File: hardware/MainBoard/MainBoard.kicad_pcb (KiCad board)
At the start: 4 copper layers, 28 x 58.4 mm, 53 parts, among them J1 Conn_02x16_Top_Bottom, J2 Conn_02x16_Top_Bottom, J3 USB_C_Receptacle_USB2.0_16P, J4 En_A, J5 En_B, J6 Micro_SD_Card_Det2, J7 Conn_02x16_Top_Bottom, Q1 MMBT2222A, U2 AMS1117-3.3, U3 AMS1117-5.0

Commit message: made boards actually square lmao
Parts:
- renumbered ESP32-S3-WROOM-1 to U1
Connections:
- C10 pad 1: CONN_VCC -> VCC_5V
- C11 pad 1: CONN_VCC -> VCC_5V
- C12 pad 1: CONN_VCC -> VCC_5V
- D4 pad 1: CONN_VCC -> VCC_5V
- Q1 pad 3: CONN_VCC -> VCC_5V
- R3 pad 1: CONN_VCC -> VCC_5V
- U3 pad 2: CONN_VCC -> VCC_5V
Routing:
- net CONN_VCC: track 103.0 -> 67.3 mm, vias 15 -> 14
- net VCC_5V: track 0.00 -> 7.69 mm, vias 0 -> 1
- added copper zone on In1.Cu, net CONN_GND
- added copper zone on In2.Cu, net CONN_VCC
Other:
- outline, holes or cut-outs redrawn

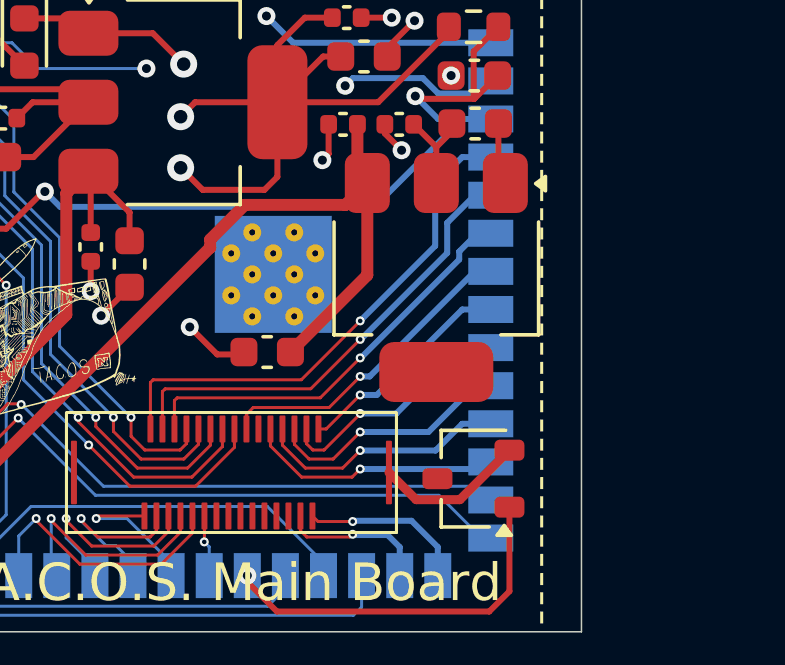
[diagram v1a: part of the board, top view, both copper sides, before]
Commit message: finished main board w/ ground and power planes
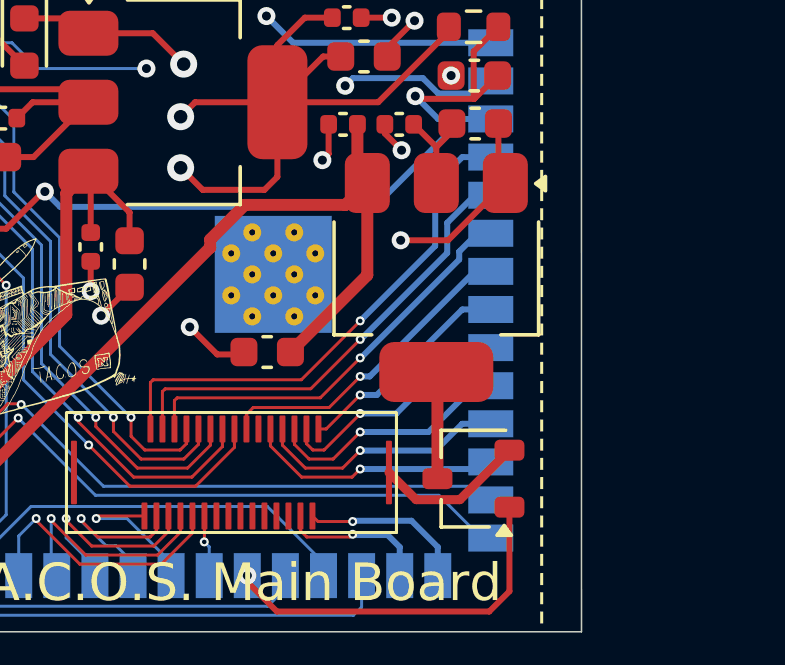
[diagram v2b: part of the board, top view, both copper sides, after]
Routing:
- net CONN_GND: track 88.8 -> 93.0 mm, vias 30 -> 31
- net VCC_5V: track 7.69 -> 11.2 mm
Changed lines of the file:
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@@
+	)
+	(segment
+		(start 87.9628 61.3156)
+		(end 86.0534 63.225)
+		(width 0.2)
+		(layer "F.Cu")
+		(net 70)
 	)
 	(segment
@@
 		(start 67.7416 90.0616)
 		(end 67.36 89.68)
+		(width 0.2)
+		(layer "F.Cu")
+		(net 70)
+	)
+	(segment
+		(start 86.0534 63.225)
+		(end 84.475 63.225)
 		(width 0.2)
 		(layer "F.Cu")
@@
 	)
 	(via
+		(at 84.475 63.225)
+		(size 0.6)
+		(drill 0.3)
+		(layers "F.Cu" "B.Cu")
+		(net 70)
+	)
+	(via
 		(at 67.29 97.55)
 		(size 0.3)
@@
 	)
 	(segment
+		(start 85.6628 60.1156)
+		(end 84.907 59.3598)
+		(width 0.2)
+		(layer "F.Cu")
+		(net 76)
+	)
+	(segment
+		(start 65.3542 91.4654)
+		(end 64.6938 90.805)
+		(width 0.2)
+		(layer "F.Cu")
+		(net 76)
+	)
+	(segment
+		(start 66.294 88.519)
+		(end 66.294 87.336)
+		(width 0.2)
+		(layer "F.Cu")
+		(net 76)
+	)
+	(segment
+		(start 86.1822 59.3344)
+		(end 86.1822 59.5962)
+		(width 0.2)
+		(layer "F.Cu")
+		(net 76)
+	)
+	(segment
+		(start 65.3542 92.329)
+		(end 65.3542 91.4654)
+		(width 0.2)
+		(layer "F.Cu")
+		(net 76)
+	)
+	(segment
+		(start 85.6628 61.3156)
+		(end 85.6628 60.1156)
+		(width 0.2)
+		(layer "F.Cu")
+		(net 76)
+	)
+	(segment
+		(start 66.294 87.336)
+		(end 67.28 86.35)
+		(width 0.2)
+		(layer "F.Cu")
+		(net 76)
+	)
+	(segment
+		(start 85.7003 71.1708)
+		(end 85.7003 67.6531)
+		(width 0.4)
+		(layer "F.Cu")
+		(net 76)
+	)
+	(segment
 		(start 85.7003 67.6531)
 		(end 85.6628 67.6156)
-		(width 0.2)
+		(width 0.4)
 		(layer "F.Cu")
 		(net 76)
-	)
-	(segment
-		(start 85.6628 60.1156)
-		(end 84.907 59.3598)
-		(width 0.2)
-		(layer "F.Cu")
-		(net 76)
-	)
-	(segment
-		(start 65.3542 91.4654)
-		(end 64.6938 90.805)
-		(width 0.2)
-		(layer "F.Cu")
-		(net 76)
-	)
-	(segment
-		(start 66.294 88.519)
-		(end 66.294 87.336)
-		(width 0.2)
-		(layer "F.Cu")
-		(net 76)
-	)
-	(segment
-		(start 86.1822 59.3344)
-		(end 86.1822 59.5962)
-		(width 0.2)
-		(layer "F.Cu")
-		(net 76)
-	)
-	(segment
-		(start 65.3542 92.329)
-		(end 65.3542 91.4654)
-		(width 0.2)
-		(layer "F.Cu")
-		(net 76)
-	)
-	(segment
-		(start 85.6628 61.3156)
-		(end 85.6628 60.1156)
-		(width 0.2)
-		(layer "F.Cu")
-		(net 76)
-	)
-	(segment
-		(start 66.294 87.336)
-		(end 67.28 86.35)
-		(width 0.2)
-		(layer "F.Cu")
-		(net 76)

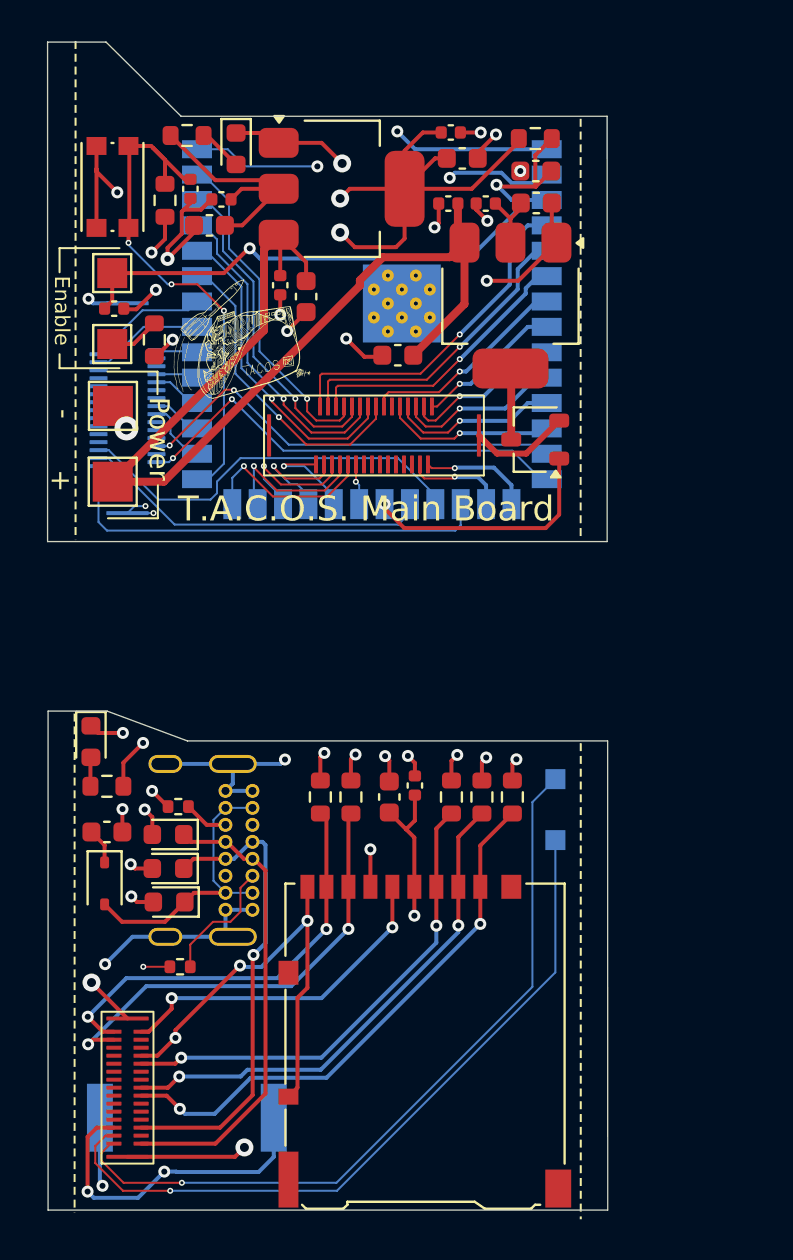
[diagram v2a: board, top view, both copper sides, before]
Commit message: added USB power switching
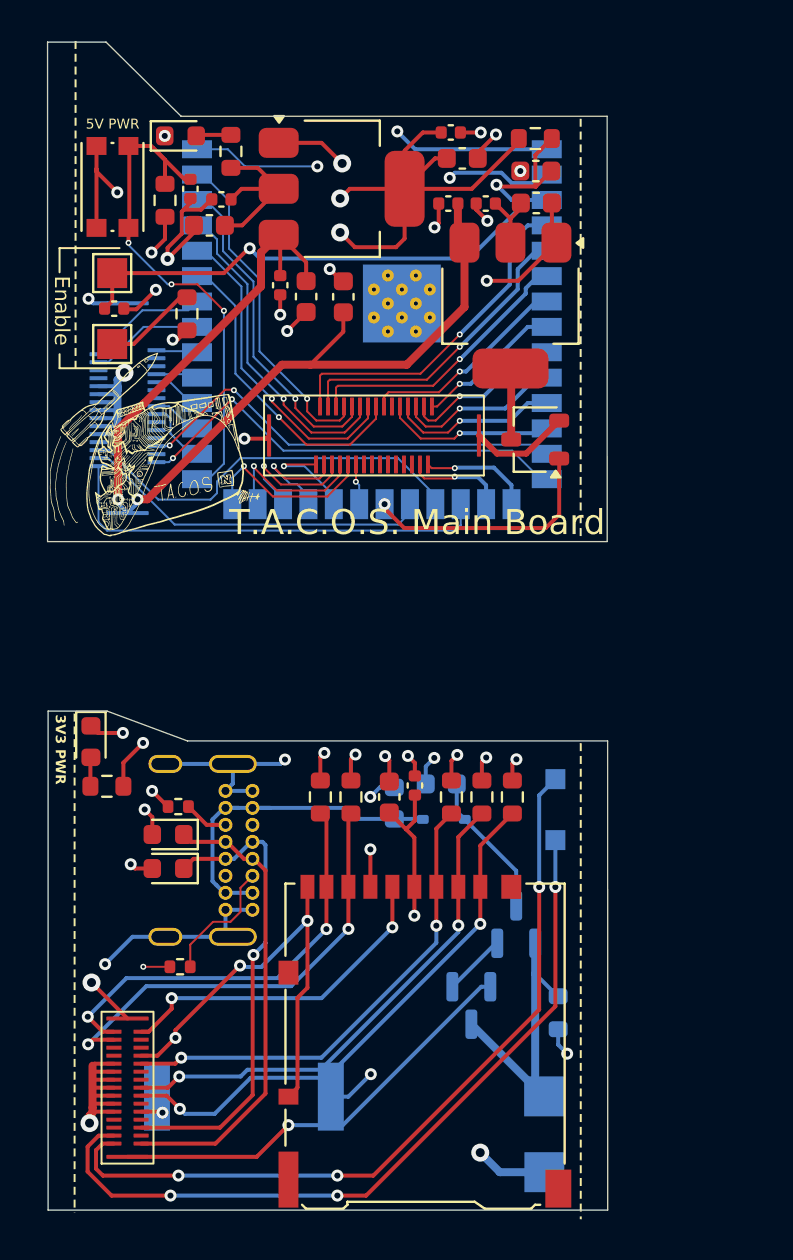
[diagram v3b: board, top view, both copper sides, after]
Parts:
- added Q2: FDN340P, Package_TO_SOT_SMD:SOT-23, B.Cu at (86.0, 95.4)
- added Q3: FDN340P, Package_TO_SOT_SMD:SOT-23, B.Cu at (83.7, 99.5)
- added R13: 10K, Resistor_SMD:R_0603_1608Metric, B.Cu at (88.0, 99.8)
- +1, -1, C12, D3, D4: moved to B.Cu
- moved -1 44.0 mm to (87.4, 107.8)
- moved +1 37.6 mm to (87.3, 104.0)
- moved D4 17.3 mm to (82.3, 90.2), turned to 180 degrees
- moved C12 16.9 mm to (82.2, 88.4), turned to 180 degrees
- moved D3 12.3 mm to (79.8, 89.4), turned to 90 degrees
- moved G*** 6.85 mm to (70.8, 61.8)
- moved C8 4.00 mm to (77.3, 64.0), turned to 90 degrees
- moved BZ1 3.04 mm to (72.3, 104.0), turned to 0 degrees
- moved D1 2.86 mm to (69.2, 56.0), turned to 0 degrees
- moved G*** 2.80 mm to (75.3, 85.0)
- moved R2 2.33 mm to (71.7, 56.8), turned to 90 degrees
- moved R12 2.09 mm to (69.5, 64.9)
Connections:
- net CONN_GND renamed LIPO GND
- C12 pad 1: VCC_5V -> VBUS
- C13 pad 1: CONN_VCC -> CONN_19
- C15 pad 1: CONN_VCC -> CONN_19
- C2 pad 1: CONN_VCC -> CONN_19
- C3 pad 1: CONN_VCC -> CONN_19
- C4 pad 1: LIPO PWR -> VIN
- C5 pad 1: LIPO PWR -> VIN
- C6 pad 1: CONN_VCC -> CONN_19
- C7 pad 1: CONN_VCC -> CONN_19
- C8 pad 1: LIPO PWR -> VIN
- C9 pad 1: LIPO PWR -> VIN
- D4 pad 1: VCC_5V -> VBUS
- J1 pad 18: BZR -> CONN_17
- J1 pad 21: CONN_20 -> CONN_19
- J1 pad 22: CONN_21 -> CONN_19
- J1 pad 23: CONN_22 -> CONN_19
- J1 pad 24: CONN_23 -> CONN_19
- J1 pad 25: CONN_24 -> CONN_19
- J1 pad 26: CONN_25 -> CONN_19
- J1 pad 31: CONN_VCC -> VIN
- J1 pad 5: CONN_4 -> BZR
- J2 pad 10: CONN_24 -> CONN_19
- J2 pad 11: CONN_25 -> CONN_19
- J2 pad 20: CONN_4 -> BZR
- J2 pad 3: BZR -> CONN_17
- J2 pad 31: CONN_VCC -> VIN
- J2 pad 6: CONN_20 -> CONN_19
- J2 pad 7: CONN_21 -> CONN_19
- J2 pad 8: CONN_22 -> CONN_19
- J2 pad 9: CONN_23 -> CONN_19
- J6 pad 4: CONN_VCC -> CONN_19
- J7 pad 31: CONN_5V -> VCC_5V
- R1 pad 1: CONN_VCC -> CONN_19
- R10 pad 1: CONN_VCC -> CONN_19
- R11 pad 1: CONN_VCC -> CONN_19
- R12 pad 1: CONN_VCC -> CONN_19
- R2 pad 1: CONN_VCC -> CONN_19
- R6 pad 1: CONN_VCC -> CONN_19
- R7 pad 1: CONN_VCC -> CONN_19
- R8 pad 1: CONN_VCC -> CONN_19
- R9 pad 1: CONN_VCC -> CONN_19
- U1 pad 2: CONN_VCC -> CONN_19
- U2 pad 2: CONN_VCC -> CONN_19
- U2 pad 3: LIPO PWR -> VIN
- U3 pad 3: LIPO PWR -> VIN
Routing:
- net CONN_19: track 0.00 -> 76.0 mm, vias 0 -> 13
- net VIN: track 0.00 -> 74.6 mm, vias 0 -> 3
- net CONN_VCC: track 67.3 -> 0.00 mm, vias 14 -> 0
- net LIPO PWR: track 52.5 -> 14.6 mm
- net BZR: track 36.8 -> 21.4 mm, vias 2 -> 1
- net VBUS: track 0.00 -> 7.33 mm
- net Net-(D3-A1): track 14.5 -> 17.9 mm
- net +5V: track 0.00 -> 3.15 mm
- net CONN_16: track 54.4 -> 56.6 mm, vias 1 -> 3
- net Net-(J4-Pin_1): track 2.54 -> 4.71 mm
- net VCC_5V: track 11.2 -> 9.41 mm
- net CONN_15: track 60.4 -> 61.9 mm, vias 1 -> 3
- net LIPO GND: track 93.0 -> 93.7 mm, vias 31 -> 34
- added copper zone on In2.Cu, net CONN_19
- removed copper zone on In2.Cu, net CONN_VCC
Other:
- board text added: "3V3 PWR"
- board text added: "5V PWR"
- board text added: "CLK"
- board text added: "DAT"
- board text added: "ESP32-S3-WROOM-1"
- board text added: "I2C"

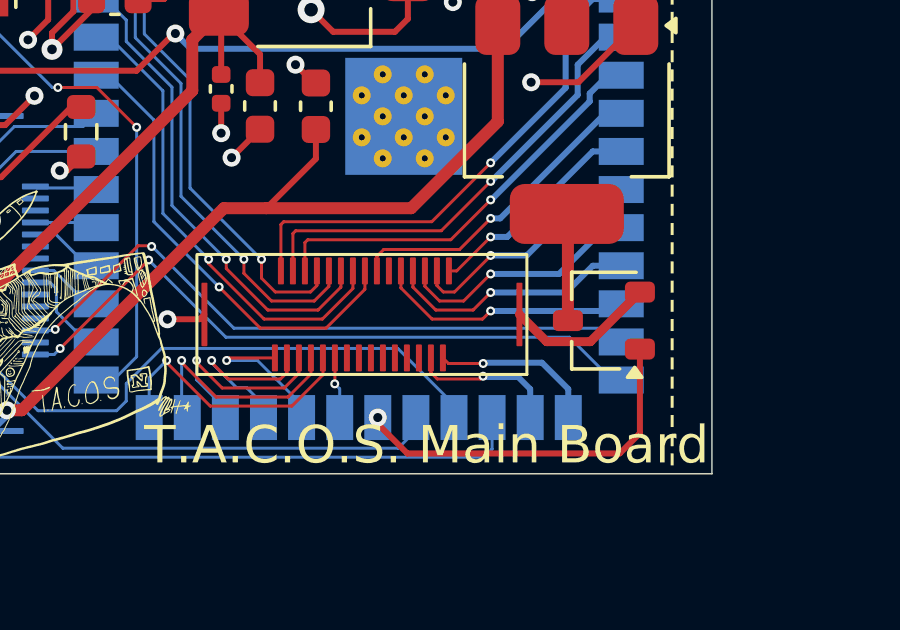
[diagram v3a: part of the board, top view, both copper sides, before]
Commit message: added power passthrough via data pins WTFFFF
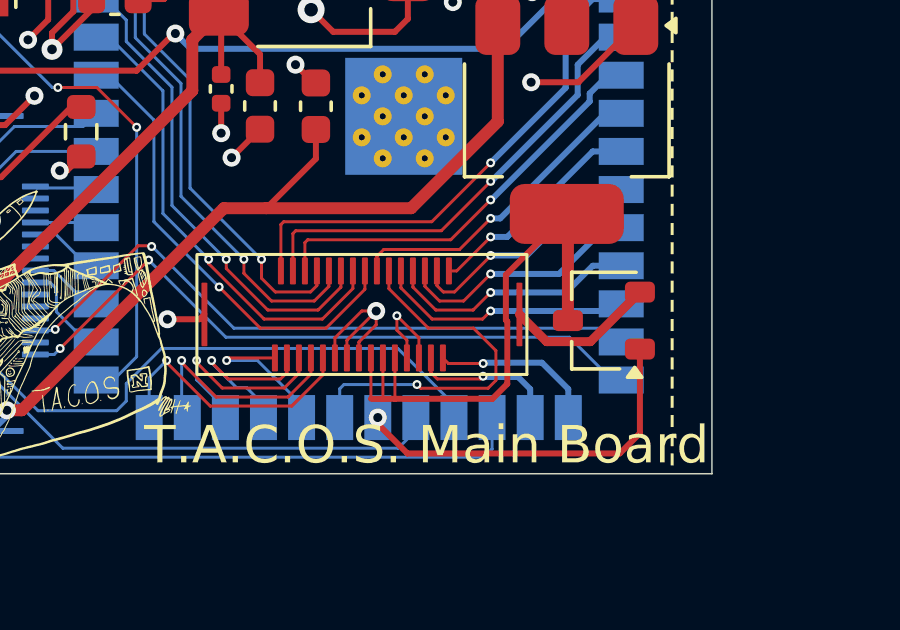
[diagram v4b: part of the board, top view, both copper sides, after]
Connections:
- J1 pad 31: VIN -> LIPO GND
- J2 pad 31: VIN -> LIPO GND
- J7 pad 18: unconnected-(J7-Pin_18-Pad18) -> LIPO GND
- J7 pad 19: unconnected-(J7-Pin_19-Pad19) -> LIPO GND
- J7 pad 20: unconnected-(J7-Pin_20-Pad20) -> VCC_5V
- J7 pad 21: unconnected-(J7-Pin_21-Pad21) -> VCC_5V
- J7 pad 22: unconnected-(J7-Pin_22-Pad22) -> VCC_5V
- J7 pad 23: unconnected-(J7-Pin_23-Pad23) -> CONN_19
- J7 pad 24: unconnected-(J7-Pin_24-Pad24) -> CONN_19
- J7 pad 25: RET -> CONN_19
- J7 pad 31: VCC_5V -> LIPO GND
- J7 pad 6: unconnected-(J7-Pin_6-Pad6) -> RET
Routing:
- net VCC_5V: track 9.41 -> 24.8 mm
- net RET: track 2.06 -> 12.4 mm
- net CONN_19: track 76.0 -> 82.2 mm, vias 13 -> 14
- net LIPO GND: track 93.7 -> 97.0 mm, vias 34 -> 35

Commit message: fixed main hat
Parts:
- removed D2: PWRLED, LED_SMD:LED_0603_1608Metric
- removed Q1: MMBT2222A, Package_TO_SOT_SMD:SOT-23W
- removed R3: 75, Resistor_SMD:R_0603_1608Metric
- added U4: TPS22917DBV, Package_TO_SOT_SMD:SOT-23-6, F.Cu at (66.1, 72.9)
- added U5: TPS22917DBV, Package_TO_SOT_SMD:SOT-23-6, F.Cu at (86.5, 73.0)
- U1: footprint RF_Module:ESP32-S3-WROOM-1 -> RF_Module:ESP32-S3-WROOM-1U
- moved D1 5.47 mm to (64.7, 52.8), turned to -90 degrees
- moved U1 3.15 mm to (78.7, 65.0)
- moved J6 0.47 mm to (81.4, 100.8)
- moved U2 0.18 mm to (77.2, 58.8)
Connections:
- C13 pad 1: CONN_19 -> CONN_18
- C15 pad 1: CONN_19 -> CONN_18
- C2 pad 1: CONN_19 -> CONN_18
- C3 pad 1: CONN_19 -> CONN_18
- C4 pad 1: VIN -> CONN_21
- C5 pad 1: VIN -> CONN_21
- C6 pad 1: CONN_19 -> CONN_18
- C7 pad 1: CONN_19 -> CONN_18
- C8 pad 1: VIN -> CONN_21
- C9 pad 1: VIN -> CONN_21
- J1 pad 20: CONN_19 -> CONN_18
- J1 pad 21: CONN_19 -> CONN_18
- J1 pad 22: CONN_19 -> CONN_21
- J1 pad 23: CONN_19 -> CONN_21
- J1 pad 24: CONN_19 -> CONN_21
- J1 pad 25: CONN_19 -> CONN_21
- J1 pad 26: CONN_19 -> CONN_21
- J1 pad 27: CONN_26 -> CONN_21
- J2 pad 10: CONN_19 -> CONN_21
- J2 pad 11: CONN_19 -> CONN_21
- J2 pad 12: CONN_26 -> CONN_21
- J2 pad 5: CONN_19 -> CONN_18
- J2 pad 6: CONN_19 -> CONN_18
- J2 pad 7: CONN_19 -> CONN_21
- J2 pad 8: CONN_19 -> CONN_21
- J2 pad 9: CONN_19 -> CONN_21
- J6 pad 4: CONN_19 -> CONN_18
- J7 pad 20: VCC_5V -> CONN_5V
- J7 pad 21: VCC_5V -> CONN_5V
- J7 pad 22: VCC_5V -> CONN_5V
- J7 pad 23: CONN_19 -> CONN_3V3
- J7 pad 24: CONN_19 -> CONN_3V3
- J7 pad 25: CONN_19 -> CONN_3V3
- Q3 pad 2: VIN -> CONN_21
- R1 pad 1: CONN_19 -> CONN_18
- R10 pad 1: CONN_19 -> CONN_18
- R11 pad 1: CONN_19 -> CONN_18
- R12 pad 1: CONN_19 -> CONN_18
- R2 pad 1: CONN_19 -> CONN_18
- R6 pad 1: CONN_19 -> CONN_18
- R7 pad 1: CONN_19 -> CONN_18
- R8 pad 1: CONN_19 -> CONN_18
- R9 pad 1: CONN_19 -> CONN_18
- U1 pad 2: CONN_19 -> CONN_18
- U2 pad 2: CONN_19 -> CONN_18
- U2 pad 3: VIN -> CONN_21
- U3 pad 3: VIN -> CONN_21
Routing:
- net CONN_21: track 0.00 -> 82.9 mm, vias 0 -> 3
- net CONN_19: track 82.2 -> 0.00 mm, vias 14 -> 0
- net VIN: track 74.6 -> 0.00 mm, vias 3 -> 0
- net CONN_18: track 0.00 -> 66.9 mm, vias 0 -> 13
- net LIPO GND: track 97.0 -> 128.2 mm, vias 35 -> 42
- net CONN_3V3: track 0.00 -> 16.0 mm
- net HATS_ENABLE: track 12.4 -> 23.5 mm, vias 1 -> 3
- net VCC_5V: track 24.8 -> 16.1 mm, vias 1 -> 0
- net CONN_5V: track 5.08 -> 13.2 mm
- net Net-(D1-A): track 1.76 -> 8.38 mm
- net Net-(D2-A): track 1.46 -> 0.00 mm
- net GPIO0: track 26.3 -> 25.4 mm
- added copper zone on In2.Cu, net CONN_18
- removed copper zone on In2.Cu, net CONN_19
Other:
- board text removed: "3V3 PWR"

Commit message: more main board polish
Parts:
- moved G*** 3.46 mm to (73.1, 59.3)
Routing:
- net CONN_21: vias 3 -> 2
- net CONN_11: vias 3 -> 2
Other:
- board text removed: "5V PWR"

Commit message: sanity checked, ready for production
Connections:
- net +5V renamed PWR_SELECT
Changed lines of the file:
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@@
 	(net 57 "LIPO GND")
 	(net 58 "VBUS")
-	(net 59 "+5V")
+	(net 59 "PWR_SELECT")
 	(net 60 "CONN_17")
 	(net 61 "unconnected-(U4-CT-Pad4)")
@@
 			(layers "B.Cu" "B.Mask" "B.Paste")
 			(roundrect_rratio 0.25)
-			(net 59 "+5V")
+			(net 59 "PWR_SELECT")
 			(pinfunction "G")
 			(pintype "input")
@@
 			(layers "B.Cu" "B.Mask" "B.Paste")
 			(roundrect_rratio 0.25)
-			(net 59 "+5V")
+			(net 59 "PWR_SELECT")
 			(pinfunction "S")
 			(pintype "passive")
